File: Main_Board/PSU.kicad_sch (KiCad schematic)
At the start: 14 parts, among them J3 Baterry input

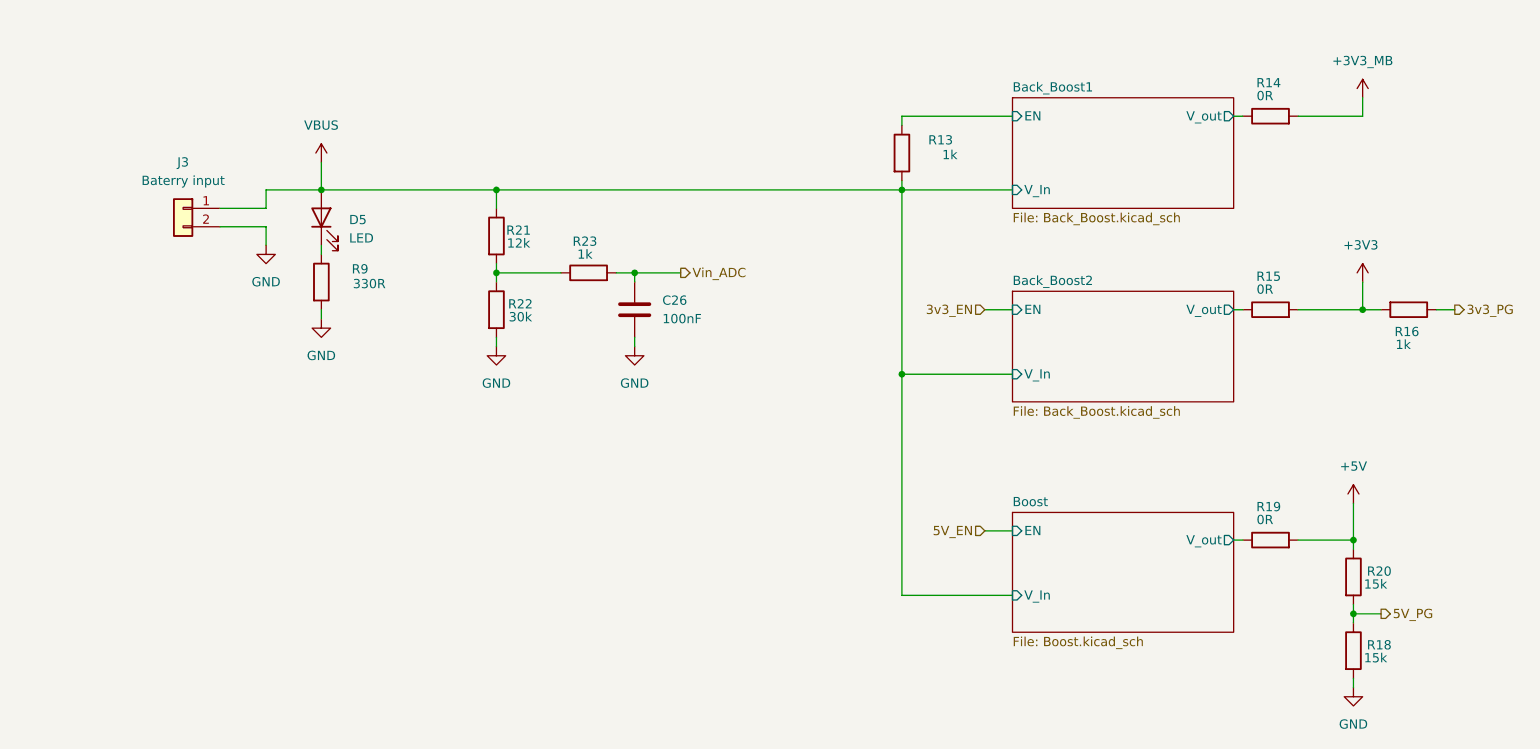
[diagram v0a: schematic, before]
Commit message: Input Protection
Irlm is left to be calculated
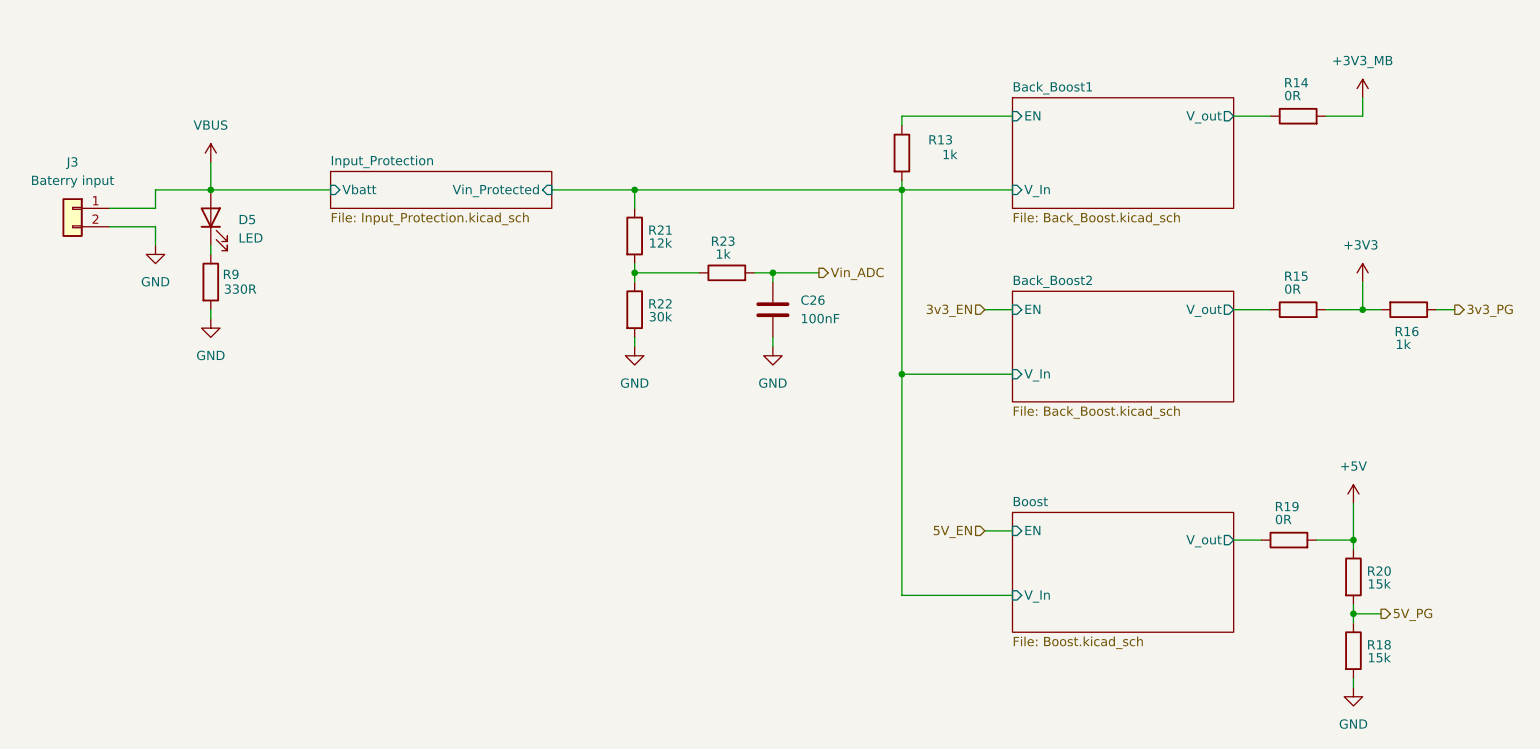
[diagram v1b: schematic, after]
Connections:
- net VBUS: no longer R13.2, R21.1
- new net Back_Boost1/V_In: R13.2, R21.1
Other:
- added sheet Input_Protection (Input_Protection.kicad_sch)
- moved on the sheet: C26, D5, J3, R14, R15, R19, R21, R22, R23, R9

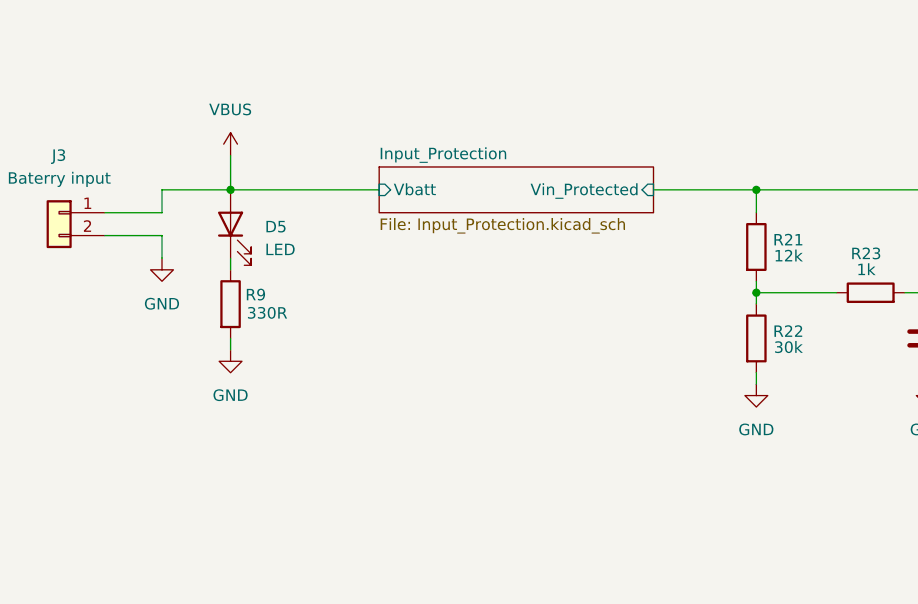
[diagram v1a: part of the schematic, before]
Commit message: Input Protection Fix
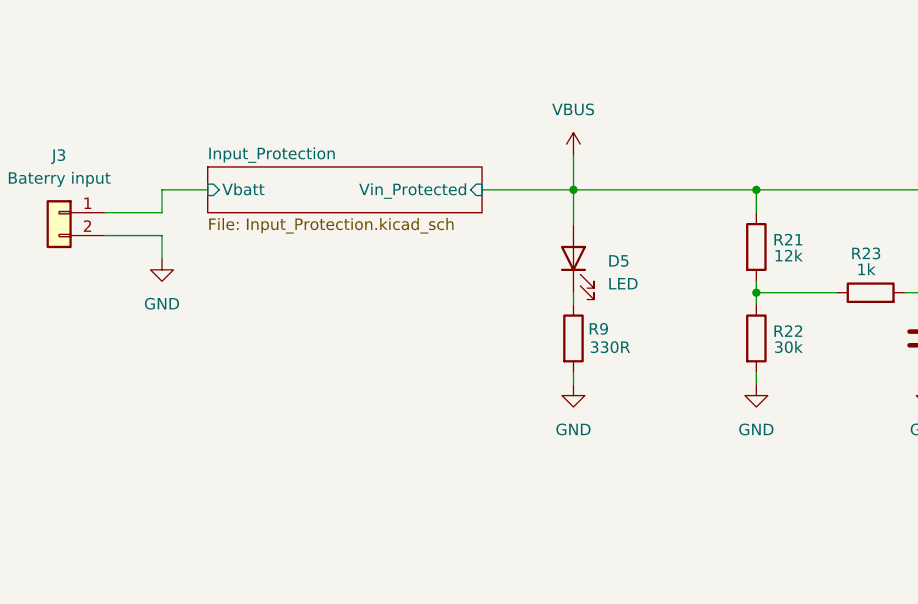
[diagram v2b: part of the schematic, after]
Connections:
- net Back_Boost1/V_In is gone; now on net VBUS: R13.2, R21.1
- net VBUS: no longer J3.1 (Pin_1)
- new net Input_Protection/Vbatt: J3.1 (Pin_1)
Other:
- moved on the sheet: D5, R9
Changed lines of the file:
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@@
 	(paper "A4")
+	(junction
+		(at 205.74 128.27)
+		(diameter 0)
+		(color 0 0 0 0)
+	)
+	(junction
+		(at 143.51 105.41)
+		(diameter 0)
+		(color 0 0 0 0)
+	)
+	(junction
+		(at 106.68 91.44)
+		(diameter 0)
+		(color 0 0 0 0)
+	)
+	(junction
+		(at 143.51 80.01)
+		(diameter 0)
+		(color 0 0 0 0)
+	)
+	(junction
+		(at 207.01 96.52)
+		(diameter 0)
+		(color 0 0 0 0)
+	)
+	(junction
+		(at 86.36 80.01)
+		(diameter 0)
+		(color 0 0 0 0)
+	)
+	(junction
+		(at 125.73 91.44)
+		(diameter 0)
+		(color 0 0 0 0)
+	)
+	(junction
+		(at 205.74 138.43)
+		(diameter 0)
+		(color 0 0 0 0)
+	)
 	(junction
 		(at 106.68 80.01)
@@
 		(color 0 0 0 0)
 	)
-	(junction
-		(at 205.74 128.27)
-		(diameter 0)
-		(color 0 0 0 0)
-	)
-	(junction
-		(at 143.51 105.41)
-		(diameter 0)
-		(color 0 0 0 0)
-	)
-	(junction
-		(at 106.68 91.44)
-		(diameter 0)
-		(color 0 0 0 0)
-	)
-	(junction
-		(at 143.51 80.01)
-		(diameter 0)
-		(color 0 0 0 0)
-	)
-	(junction
-		(at 207.01 96.52)
-		(diameter 0)
-		(color 0 0 0 0)
-	)
-	(junction
-		(at 125.73 91.44)
-		(diameter 0)
-		(color 0 0 0 0)
-	)
-	(junction
-		(at 205.74 138.43)
-		(diameter 0)
-		(color 0 0 0 0)
-	)
-	(junction
-		(at 48.26 80.01)
-		(diameter 0)
-		(color 0 0 0 0)
-	)
 	(wire
 		(pts
@@
 	(wire
 		(pts
-			(xy 95.25 80.01) (xy 106.68 80.01)
+			(xy 76.2 80.01) (xy 86.36 80.01)
 		)
 		(stroke
@@
 	(wire
 		(pts
+			(xy 86.36 80.01) (xy 86.36 83.82)
+		)
+		(stroke
+			(width 0)
+			(type default)
+		)
+	)
+	(wire
+		(pts
 			(xy 205.74 137.16) (xy 205.74 138.43)
 		)
@@
 	(wire
 		(pts
-			(xy 40.64 80.01) (xy 48.26 80.01)
+			(xy 40.64 80.01) (xy 45.72 80.01)
 		)
 		(stroke
@@
 	(wire
 		(pts
-			(xy 48.26 88.9) (xy 48.26 87.63)
+			(xy 86.36 92.71) (xy 86.36 91.44)
 		)
 		(stroke
@@
 	(wire
 		(pts
+			(xy 86.36 76.2) (xy 86.36 80.01)
+		)
+		(stroke
+			(width 0)
+			(type default)
+		)
+	)
+	(wire
+		(pts
 			(xy 143.51 78.74) (xy 143.51 80.01)
 		)
@@
 	(wire
 		(pts
-			(xy 48.26 80.01) (xy 48.26 76.2)
-		)
-		(stroke
-			(width 0)
-			(type default)
-		)
-	)
-	(wire
-		(pts
 			(xy 207.01 92.71) (xy 207.01 96.52)
 		)
@@
 	(wire
 		(pts
-			(xy 48.26 80.01) (xy 64.77 80.01)
-		)
-		(stroke
-			(width 0)
-			(type default)
-		)
-	)
-	(wire
-		(pts
-			(xy 48.26 96.52) (xy 48.26 97.79)
+			(xy 86.36 100.33) (xy 86.36 101.6)
 		)
 		(stroke
@@
 		(pts
 			(xy 106.68 80.01) (xy 106.68 82.55)
+		)
+		(stroke
+			(width 0)
+			(type default)
+		)
+	)
+	(wire
+		(pts
+			(xy 86.36 80.01) (xy 106.68 80.01)
 		)
 		(stroke
@@
 	(symbol
 		(lib_id "power:GND")
-		(at 48.26 97.79 0)
+		(at 86.36 101.6 0)
 		(unit 1)
 		(body_style 1)
@@
 		(fields_autoplaced yes)
 		(property "Reference" "#PWR043"
-			(at 48.26 104.14 0)
+			(at 86.36 107.95 0)
 			(hide yes)
 			(show_name no)
@@
 		)
 		(property "Value" "GND"
-			(at 48.26 102.87 0)
+			(at 86.36 106.68 0)
 			(show_name no)
 			(do_not_autoplace no)
@@
 		)
 		(property "Footprint" ""
-			(at 48.26 97.79 0)
+			(at 86.36 101.6 0)
 			(hide yes)
 			(show_name no)
@@
 		)
 		(property "Datasheet" ""
-			(at 48.26 97.79 0)
+			(at 86.36 101.6 0)
 			(hide yes)
 			(show_name no)
@@
 		)
 		(property "Description" "Power symbol creates a global label with name \"GND\" , ground"
-			(at 48.26 97.79 0)
+			(at 86.36 101.6 0)
 			(hide yes)
 			(show_name no)
@@
 	(symbol
 		(lib_id "Device:R")
-		(at 48.26 92.71 0)
+		(at 86.36 96.52 0)
 		(unit 1)
 		(body_style 1)
@@
 		(dnp no)
 		(property "Reference" "R9"
-			(at 51.054 91.694 0)
+			(at 89.154 95.504 0)
 			(show_name no)
 			(do_not_autoplace no)
@@
 		)
 		(property "Value" "330R"
-			(at 52.324 93.726 0)
+			(at 90.424 97.536 0)
 			(show_name no)
 			(do_not_autoplace no)
@@
 		)
 		(property "Footprint" ""
-			(at 46.482 92.71 90)
+			(at 84.582 96.52 90)
 			(hide yes)
 			(show_name no)
@@
 		)
 		(property "Datasheet" ""
-			(at 48.26 92.71 0)
+			(at 86.36 96.52 0)
 			(hide yes)
 			(show_name no)
@@
 		)
 		(property "Description" "Resistor"
-			(at 48.26 92.71 0)
+			(at 86.36 96.52 0)
 			(hide yes)
 			(show_name no)
@@
 	(symbol
 		(lib_id "power:VBUS")
-		(at 48.26 76.2 0)
+		(at 86.36 76.2 0)
 		(unit 1)
 		(body_style 1)
@@
 		(fields_autoplaced yes)
 		(property "Reference" "#PWR024"
-			(at 48.26 80.01 0)
+			(at 86.36 80.01 0)
 			(hide yes)
 			(show_name no)
@@
 		)
 		(property "Value" "VBUS"
-			(at 48.26 71.12 0)
+			(at 86.36 71.12 0)
 			(show_name no)
 			(do_not_autoplace no)
@@
 		)
 		(property "Footprint" ""
-			(at 48.26 76.2 0)
+			(at 86.36 76.2 0)
 			(hide yes)
 			(show_name no)
@@
 		)
 		(property "Datasheet" ""
-			(at 48.26 76.2 0)
+			(at 86.36 76.2 0)
 			(hide yes)
 			(show_name no)
@@
 		)
 		(property "Description" "Power symbol creates a global label with name \"VBUS\""
-			(at 48.26 76.2 0)
+			(at 86.36 76.2 0)
 			(hide yes)
 			(show_name no)
@@
 	(symbol
 		(lib_id "Device:LED")
-		(at 48.26 83.82 90)
+		(at 86.36 87.63 90)
 		(unit 1)
 		(body_style 1)
@@
 		(fields_autoplaced yes)
 		(property "Reference" "D5"
-			(at 52.07 84.1374 90)
+			(at 90.17 87.9474 90)
 			(show_name no)
 			(do_not_autoplace no)
@@
 		)
 		(property "Value" "LED"
-			(at 52.07 86.6774 90)
+			(at 90.17 90.4874 90)
 			(show_name no)
 			(do_not_autoplace no)
@@
 		)
 		(property "Footprint" ""
-			(at 48.26 83.82 0)
+			(at 86.36 87.63 0)
 			(hide yes)
 			(show_name no)
@@
 		)
 		(property "Datasheet" ""
-			(at 48.26 83.82 0)
+			(at 86.36 87.63 0)
 			(hide yes)
 			(show_name no)
@@
 		)
 		(property "Description" "Light emitting diode"
-			(at 48.26 83.82 0)
+			(at 86.36 87.63 0)
 			(hide yes)
 			(show_name no)
@@
 		)
 		(property "Sim.Pins" "1=K 2=A"
-			(at 48.26 83.82 0)
+			(at 86.36 87.63 0)
 			(hide yes)
 			(show_name no)
@@
 	)
 	(sheet
-		(at 64.77 77.47)
+		(at 45.72 77.47)
 		(size 30.48 5.08)
 		(exclude_from_sim no)
@@
 		)
 		(property "Sheetname" "Input_Protection"
-			(at 64.77 76.7584 0)
+			(at 45.72 76.7584 0)
 			(show_name no)
 			(do_not_autoplace no)
@@
 		)
 		(property "Sheetfile" "Input_Protection.kicad_sch"
-			(at 64.77 83.1346 0)
+			(at 45.72 83.1346 0)
 			(show_name no)
 			(do_not_autoplace no)
@@
 		)
 		(pin "Vin_Protected" input
-			(at 95.25 80.01 0)
+			(at 76.2 80.01 0)
 			(effects
 				(font
@@
 		)
 		(pin "Vbatt" input
-			(at 64.77 80.01 180)
-			(effects
-				(font
+			(at 45.72 80.01 180)
+			(effects
+				(font

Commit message: RS485 Transciever + Input Protection fix
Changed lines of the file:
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@@
 			)
 		)
-		(pin "Vin_Protected" input
+		(pin "Vin_Protected" output
 			(at 76.2 80.01 0)
 			(effects

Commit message: Aesthetics/cleanup
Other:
- moved on the sheet: D5, J3, R9
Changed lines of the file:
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@@
 	(wire
 		(pts
-			(xy 86.36 80.01) (xy 86.36 83.82)
+			(xy 86.36 80.01) (xy 86.36 82.55)
 		)
 		(stroke
@@
 	(wire
 		(pts
-			(xy 40.64 80.01) (xy 45.72 80.01)
-		)
-		(stroke
-			(width 0)
-			(type default)
-		)
-	)
-	(wire
-		(pts
 			(xy 106.68 90.17) (xy 106.68 91.44)
 		)
@@
 	(wire
 		(pts
-			(xy 86.36 92.71) (xy 86.36 91.44)
+			(xy 86.36 91.44) (xy 86.36 90.17)
 		)
 		(stroke
@@
 	(wire
 		(pts
-			(xy 34.29 85.09) (xy 40.64 85.09)
+			(xy 34.29 82.55) (xy 40.64 82.55)
 		)
 		(stroke
@@
 	(wire
 		(pts
-			(xy 34.29 82.55) (xy 40.64 82.55)
+			(xy 34.29 80.01) (xy 45.72 80.01)
 		)
 		(stroke
@@
 	(wire
 		(pts
-			(xy 86.36 100.33) (xy 86.36 101.6)
+			(xy 86.36 99.06) (xy 86.36 101.6)
 		)
 		(stroke
@@
 	(wire
 		(pts
-			(xy 40.64 82.55) (xy 40.64 80.01)
-		)
-		(stroke
-			(width 0)
-			(type default)
-		)
-	)
-	(wire
-		(pts
 			(xy 219.71 96.52) (xy 217.17 96.52)
 		)
@@
 	(wire
 		(pts
-			(xy 40.64 85.09) (xy 40.64 87.63)
+			(xy 40.64 82.55) (xy 40.64 85.09)
 		)
 		(stroke
@@
 	(symbol
 		(lib_id "Connector_Generic:Conn_01x02")
-		(at 29.21 82.55 0)
+		(at 29.21 80.01 0)
 		(mirror y)
 		(unit 1)
@@
 		(fields_autoplaced yes)
 		(property "Reference" "J3"
+			(at 29.21 73.66 0)
+			(show_name no)
+			(do_not_autoplace no)
+			(effects
+				(font
+					(size 1.27 1.27)
+				)
+			)
+		)
+		(property "Value" "Baterry input"
 			(at 29.21 76.2 0)
 			(show_name no)
@@
 			)
 		)
-		(property "Value" "Baterry input"
-			(at 29.21 78.74 0)
-			(show_name no)
-			(do_not_autoplace no)
-			(effects
-				(font
-					(size 1.27 1.27)
-				)
-			)
-		)
 		(property "Footprint" ""
-			(at 29.21 82.55 0)
+			(at 29.21 80.01 0)
 			(hide yes)
 			(show_name no)
@@
 		)
 		(property "Datasheet" ""
-			(at 29.21 82.55 0)
+			(at 29.21 80.01 0)
 			(hide yes)
 			(show_name no)
@@
 		)
 		(property "Description" "Generic connector, single row, 01x02, script generated (kicad-library-utils/schlib/autogen/connector/)"
-			(at 29.21 82.55 0)
+			(at 29.21 80.01 0)
 			(hide yes)
 			(show_name no)
@@
 	(symbol
 		(lib_id "power:GND")
-		(at 40.64 87.63 0)
+		(at 40.64 85.09 0)
 		(unit 1)
 		(body_style 1)
@@
 		(fields_autoplaced yes)
 		(property "Reference" "#PWR025"
-			(at 40.64 93.98 0)
+			(at 40.64 91.44 0)
 			(hide yes)
 			(show_name no)
@@
 		)
 		(property "Value" "GND"
-			(at 40.64 92.71 0)
+			(at 40.64 90.17 0)
 			(show_name no)
 			(do_not_autoplace no)
@@
 		)
 		(property "Footprint" ""
-			(at 40.64 87.63 0)
+			(at 40.64 85.09 0)
 			(hide yes)
 			(show_name no)
@@
 		)
 		(property "Datasheet" ""
-			(at 40.64 87.63 0)
+			(at 40.64 85.09 0)
 			(hide yes)
 			(show_name no)
@@
 		)
 		(property "Description" "Power symbol creates a global label with name \"GND\" , ground"
-			(at 40.64 87.63 0)
+			(at 40.64 85.09 0)
 			(hide yes)
 			(show_name no)
@@
 	(symbol
 		(lib_id "Device:R")
-		(at 86.36 96.52 0)
+		(at 86.36 95.25 0)
 		(unit 1)
 		(body_style 1)
@@
 		(dnp no)
 		(property "Reference" "R9"
-			(at 89.154 95.504 0)
+			(at 89.154 94.234 0)
 			(show_name no)
 			(do_not_autoplace no)
@@
 		)
 		(property "Value" "330R"
-			(at 90.424 97.536 0)
+			(at 90.424 96.266 0)
 			(show_name no)
 			(do_not_autoplace no)
@@
 		)
 		(property "Footprint" ""
-			(at 84.582 96.52 90)
+			(at 84.582 95.25 90)
 			(hide yes)
 			(show_name no)
@@
 		)
 		(property "Datasheet" ""
-			(at 86.36 96.52 0)
+			(at 86.36 95.25 0)
 			(hide yes)
 			(show_name no)
@@
 		)
 		(property "Description" "Resistor"
-			(at 86.36 96.52 0)
+			(at 86.36 95.25 0)
 			(hide yes)
 			(show_name no)
@@
 	(symbol
 		(lib_id "Device:LED")
-		(at 86.36 87.63 90)
+		(at 86.36 86.36 90)
 		(unit 1)
 		(body_style 1)
@@
 		(fields_autoplaced yes)
 		(property "Reference" "D5"
-			(at 90.17 87.9474 90)
+			(at 90.17 86.6774 90)
 			(show_name no)
 			(do_not_autoplace no)
@@
 		)
 		(property "Value" "LED"
-			(at 90.17 90.4874 90)
+			(at 90.17 89.2174 90)
 			(show_name no)
 			(do_not_autoplace no)
@@
 		)
 		(property "Footprint" ""
-			(at 86.36 87.63 0)
+			(at 86.36 86.36 0)
 			(hide yes)
 			(show_name no)
@@
 		)
 		(property "Datasheet" ""
-			(at 86.36 87.63 0)
+			(at 86.36 86.36 0)
 			(hide yes)
 			(show_name no)
@@
 		)
 		(property "Description" "Light emitting diode"
-			(at 86.36 87.63 0)
+			(at 86.36 86.36 0)
 			(hide yes)
 			(show_name no)
@@
 		)
 		(property "Sim.Pins" "1=K 2=A"
-			(at 86.36 87.63 0)
-			(hide yes)
-			(show_name no)
+			(at 86.36 86.36 0)
+			(hide yes)
+			(show_name no)
